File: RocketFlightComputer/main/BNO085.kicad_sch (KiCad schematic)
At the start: 10 parts

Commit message: Well I added a bunch of sensors, some connectors for battery, pyro channels mosfets, etc
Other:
- note added: "Max Current: 30 mA"
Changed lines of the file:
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@@
     (stroke (width 0) (type default))
+  )
+  (text "Max Current: 30 mA" (at 93.98 99.06 0)
+    (effects (font (size 1.778 1.5113)) (justify left bottom))
   )
   (text "SA0 is default low, so I2C ADDR = 1001010 (0x4A)" (at 94.615 103.505 0)

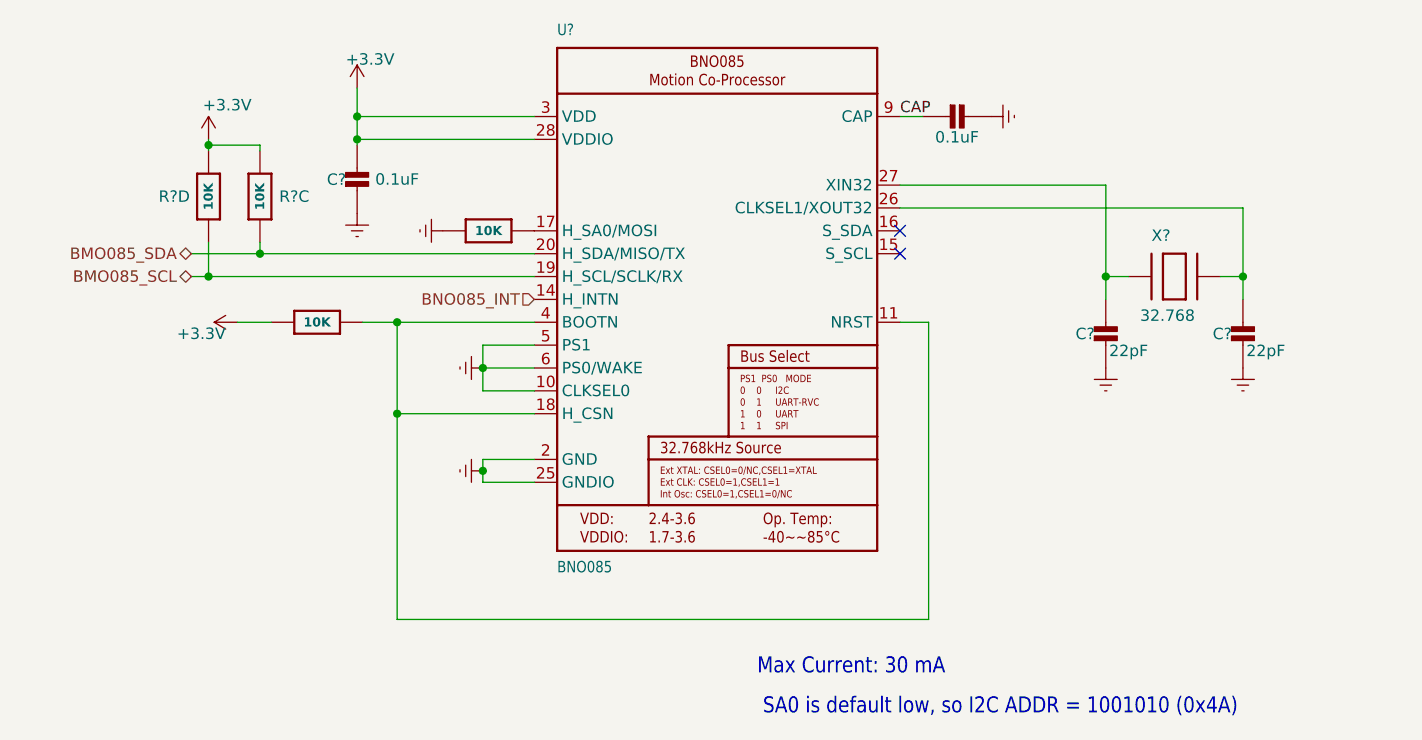
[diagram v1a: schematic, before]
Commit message: Addition of telemetry is pcb schematic
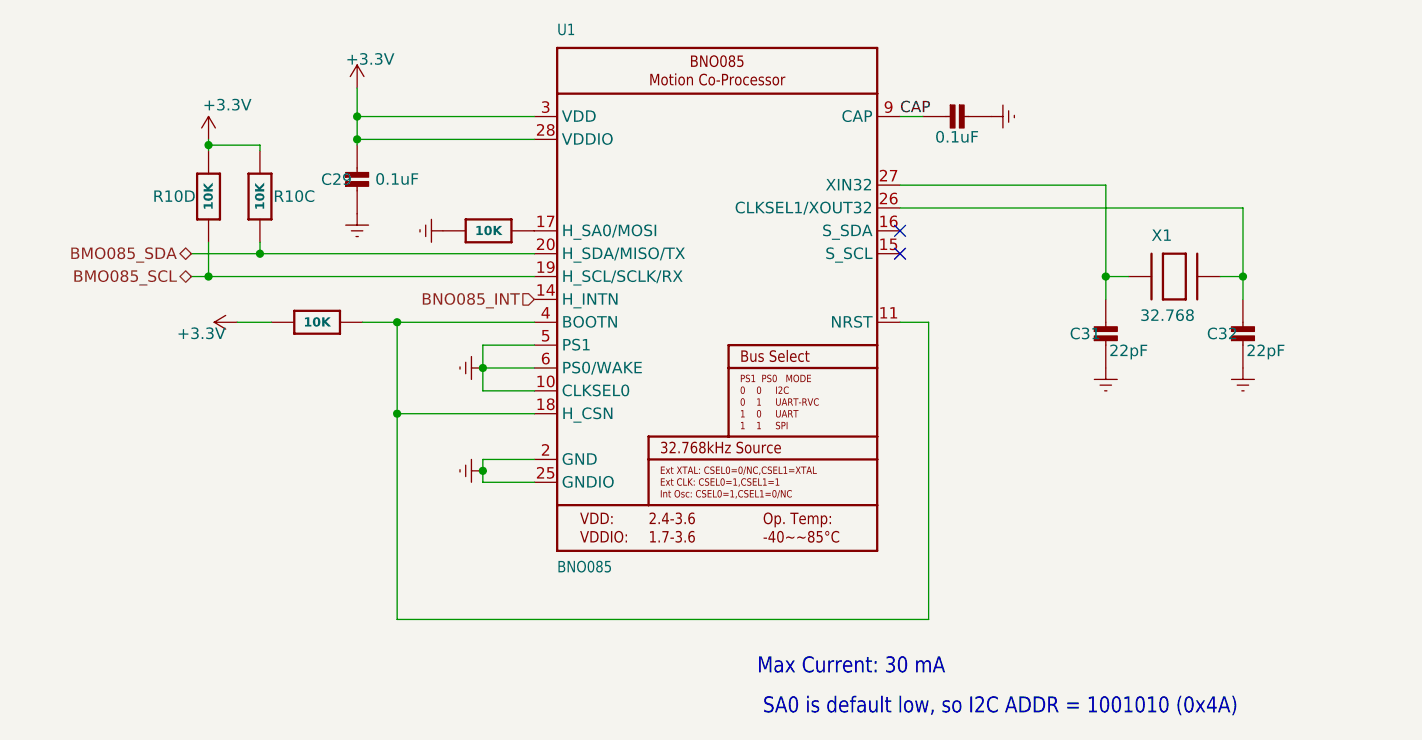
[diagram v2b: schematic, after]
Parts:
- gave numbers to parts that had none: 8

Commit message: The design is getting more mature, still did not choose if doing 4 layers or 2 layers pcb, will try to add 5v for a on board camera and trace routes for reserved pins in case of usage on another vehicle
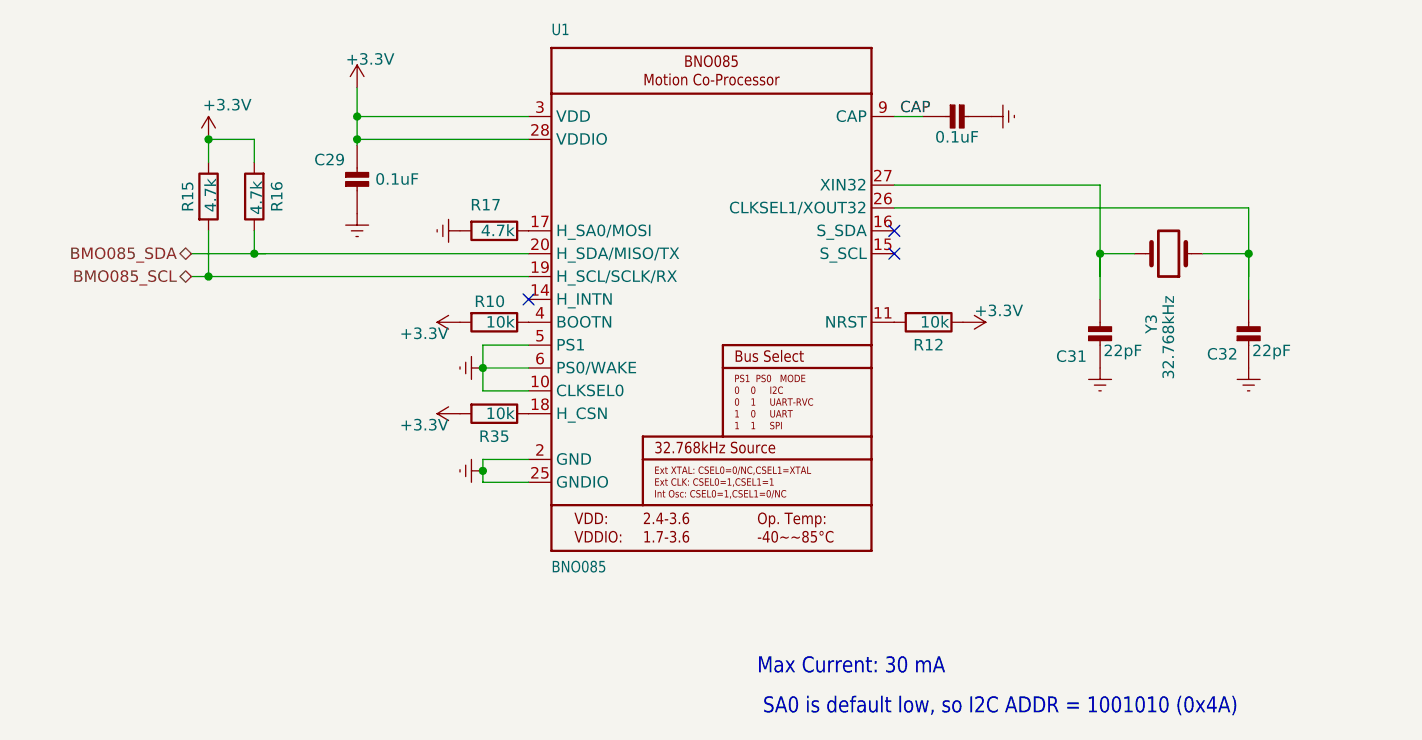
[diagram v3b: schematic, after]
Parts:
- removed R10, R11: 10K, Resistor_SMD:R_0603_1608Metric_Pad0.98x0.95mm_HandSolder, symbol Adafruit_BNO08x-eagle-import:RESISTOR_4PACK
- removed X1: 32.768, Crystal:Crystal_SMD_2012-2Pin_2.0x1.2mm, symbol Adafruit_BNO08x-eagle-import:XTAL-3.2X1.5
- added R10, R12, R35: 10k, Resistor_SMD:R_0603_1608Metric_Pad0.98x0.95mm_HandSolder, symbol Device:R
- added R15, R16, R17: 4.7k, Resistor_SMD:R_0603_1608Metric_Pad0.98x0.95mm_HandSolder, symbol Device:R
- added Y3: 32.768kHz, Crystal:Crystal_SMD_2012-2Pin_2.0x1.2mm, symbol Device:Crystal
- C32: footprint Adafruit_BNO08x:0603-NO -> Resistor_SMD:R_0603_1608Metric_Pad0.98x0.95mm_HandSolder
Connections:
- net +3.3V: now also R10.2, R12.1, R15.1, R16.2, R35.2
- net BMO085_SCL: now also R15.2
- net BMO085_SDA: now also R16.1
- net GNDREF: now also R17.2
- net at C31.1, U1.27 (XIN32): now also Y3.2
- net at C32.1, U1.26 (CLKSEL1/XOUT32): now also Y3.1
- net at U1.17 (H_SA0/MOSI): now also R17.1
- net BNO085_INT: no longer names the net of U1.14 (H_INTN)
- new net: R12.2, U1.11 (NRST)
- new net: R10.1, U1.4 (BOOTN)
- new net: R35.1, U1.18 (H_CSN)
- no-connect marks 2 -> 3
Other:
- moved on the sheet: C31, C32, U1

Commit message: Layout of PCB mostly done
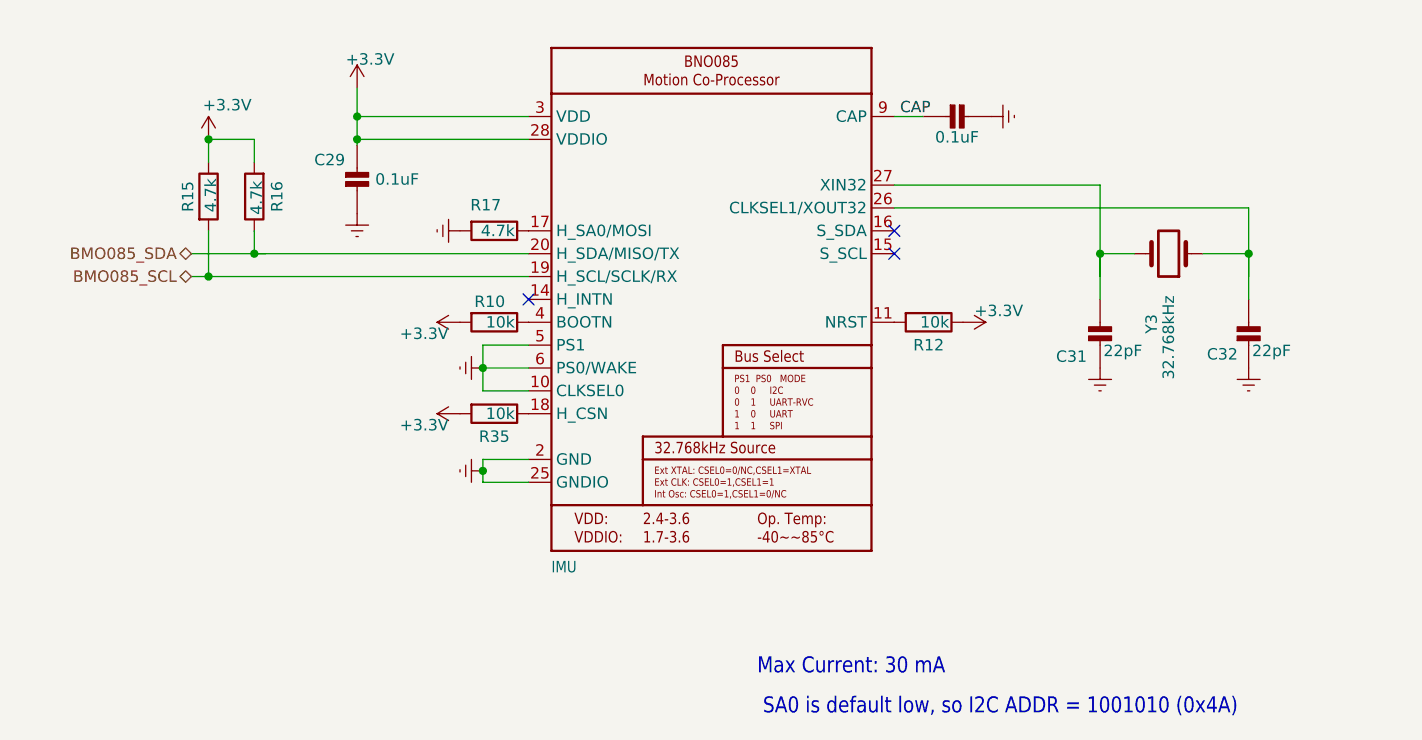
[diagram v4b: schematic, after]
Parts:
- BNO85: renamed from U1; value BNO085 -> IMU; footprint BNO08x:BNO080 -> footprint:BNO085
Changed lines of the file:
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@@
 		(on_board yes)
 		(dnp no)
-		(property "Reference" "U1"
+		(property "Reference" "BNO85"
 			(at 71.12 27.94 0)
 			(effects
@@
 				)
 				(justify left bottom)
+				(hide yes)
 			)
 		)
-		(property "Value" "BNO085"
+		(property "Value" "IMU"
 			(at 71.12 87.63 0)
 			(effects
@@
 			)
 		)
-		(property "Footprint" "BNO08x:BNO080"
+		(property "Footprint" "footprint:BNO085"
 			(at 88.9 57.15 0)
 			(effects
@@
 			(project "main"
 				(path "/27195d1d-92b2-40df-ada5-3b20841577e7/f1ce41f5-ec33-4382-82d9-21de8266ebc9"
-					(reference "U1")
+					(reference "BNO85")
 					(unit 1)
 				)

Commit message: Preliminary layout done but need to rearrange sd card and such to have the best routing
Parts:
- Y3: footprint Crystal:Crystal_SMD_2012-2Pin_2.0x1.2mm -> footprint:830050789
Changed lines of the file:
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@@
 			)
 		)
-		(property "Footprint" "Crystal:Crystal_SMD_2012-2Pin_2.0x1.2mm"
+		(property "Footprint" "footprint:830050789"
 			(at 139.7 52.07 0)
 			(effects

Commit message: Routing pcb
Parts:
- Y3: footprint footprint:830050789 -> Crystal:Crystal_SMD_2012-2Pin_2.0x1.2mm_HandSoldering
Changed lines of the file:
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@@
 			)
 		)
-		(property "Footprint" "footprint:830050789"
+		(property "Footprint" "Crystal:Crystal_SMD_2012-2Pin_2.0x1.2mm_HandSoldering"
 			(at 139.7 52.07 0)
 			(effects

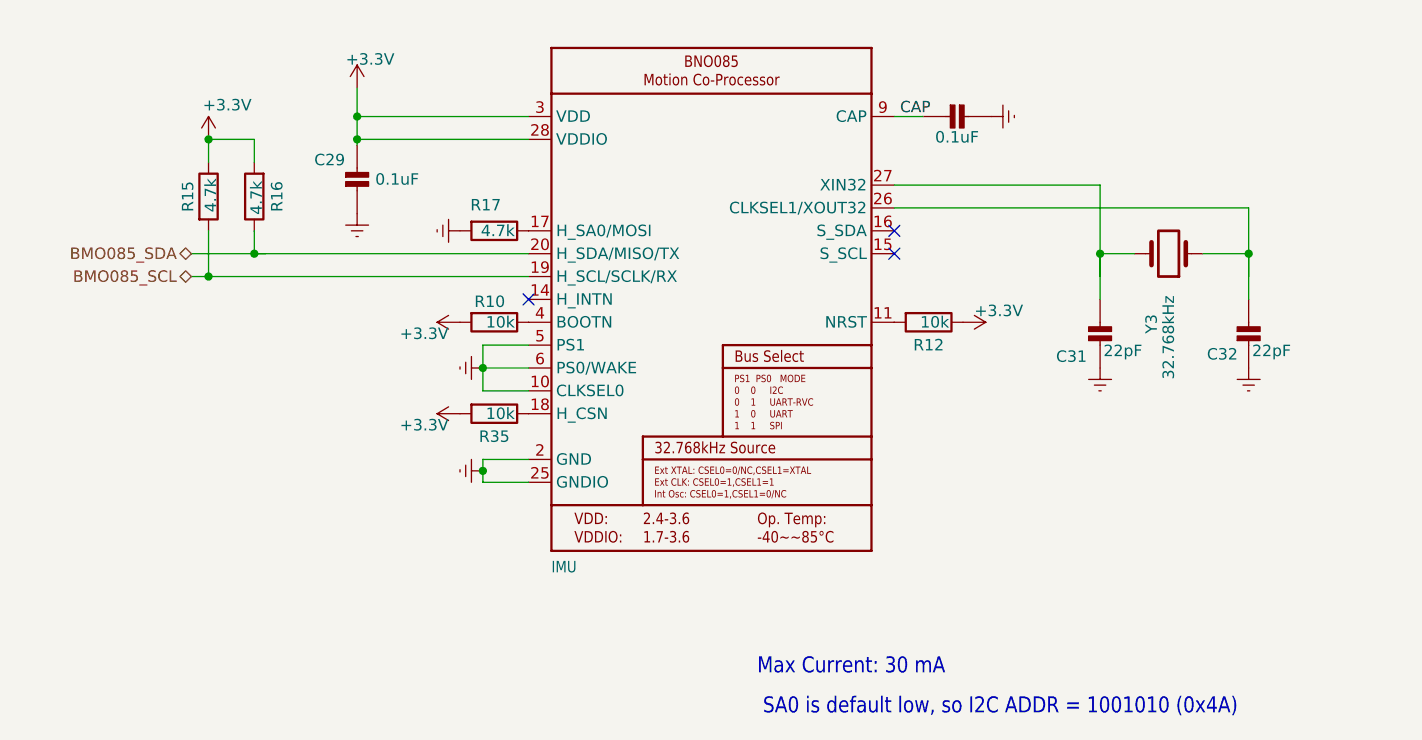
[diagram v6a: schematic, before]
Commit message: Addition of teensy example and milestone on routing completed, missing a few components to connect
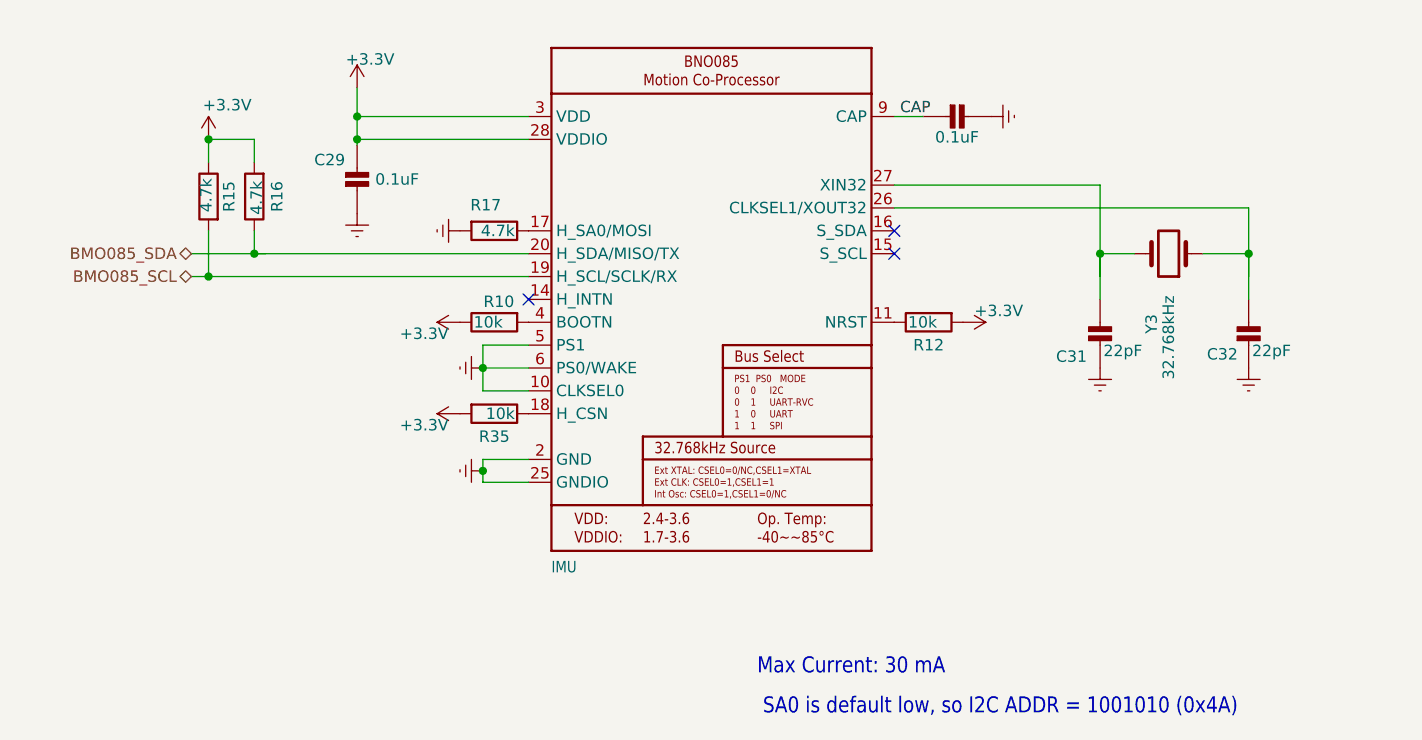
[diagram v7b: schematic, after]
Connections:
- net +3.3V: now also R10.1, R12.2; no longer R10.2, R12.1
- net at BNO85.11 (NRST): now also R12.1; no longer R12.2
- net at BNO85.4 (BOOTN): now also R10.2; no longer R10.1
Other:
- moved on the sheet: R10, R12
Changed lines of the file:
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@@
 	(symbol
 		(lib_id "Device:R")
-		(at 113.03 59.69 270)
+		(at 113.03 59.69 90)
+		(mirror x)
 		(unit 1)
 		(exclude_from_sim no)
@@
 		)
 		(property "Value" "10k"
-			(at 115.316 59.69 90)
+			(at 110.744 59.69 90)
 			(effects
 				(font
@@
 	(symbol
 		(lib_id "Device:R")
-		(at 64.77 59.69 270)
+		(at 64.77 59.69 90)
+		(mirror x)
 		(unit 1)
 		(exclude_from_sim no)
@@
 		(dnp no)
 		(property "Reference" "R10"
-			(at 64.262 57.404 90)
+			(at 65.278 57.404 90)
 			(effects
 				(font
@@
 		)
 		(property "Value" "10k"
-			(at 67.056 59.69 90)
+			(at 62.484 59.69 90)
 			(effects
 				(font
@@
 		(lib_id "Device:R")
 		(at 33.02 45.72 0)
+		(mirror y)
 		(unit 1)
 		(exclude_from_sim no)
@@
 		(dnp no)
 		(property "Reference" "R15"
-			(at 30.734 45.72 90)
+			(at 35.306 45.72 90)
 			(effects
 				(font
@@
 		)
 		(property "Value" "4.7k"
-			(at 33.274 43.688 90)
+			(at 32.766 43.688 90)
 			(effects
 				(font
@@
 		)
 		(property "Footprint" "Resistor_SMD:R_0603_1608Metric_Pad0.98x0.95mm_HandSolder"
-			(at 31.242 45.72 90)
-			(effects
-				(font
+			(at 34.798 45.72 90)
+			(effects
+				(font

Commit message: First pass of verification and validation of pcb design
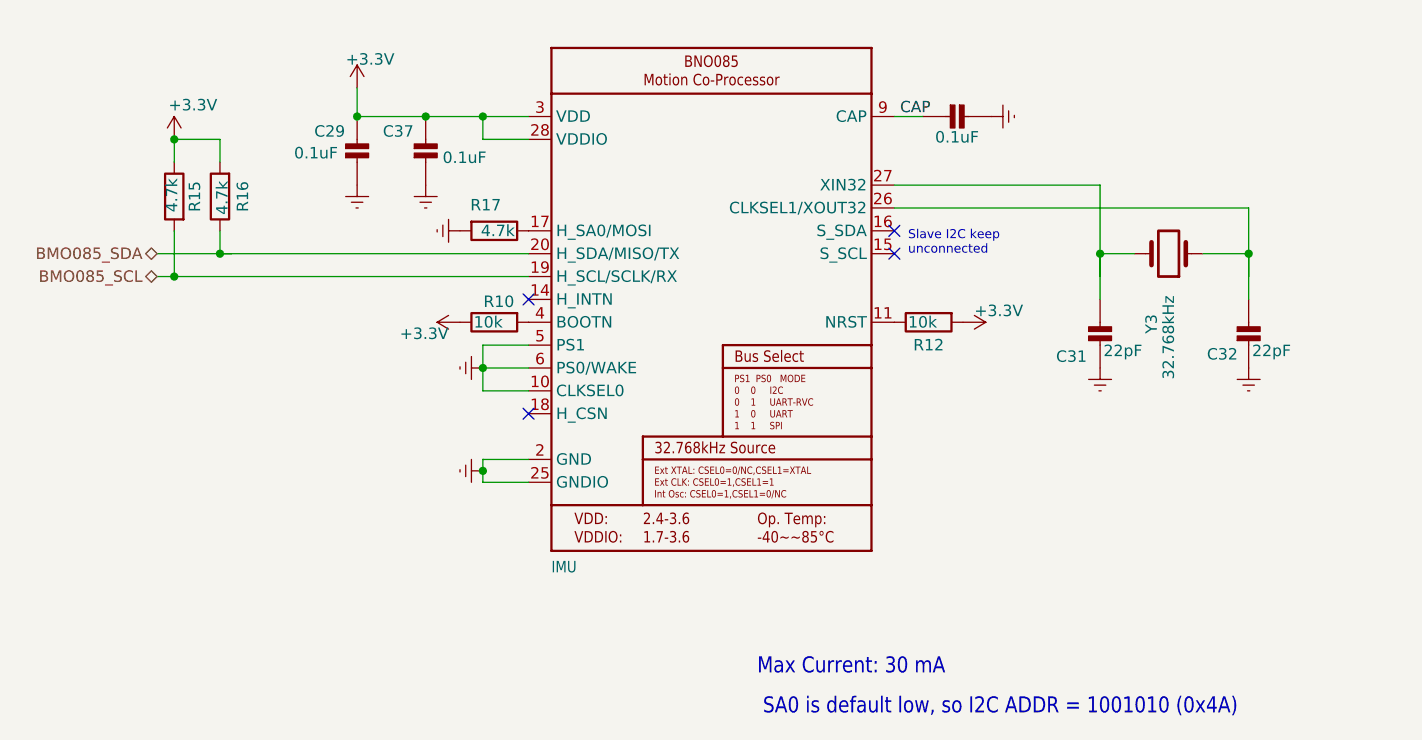
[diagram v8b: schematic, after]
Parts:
- removed R35: 10k, Resistor_SMD:R_0603_1608Metric_Pad0.98x0.95mm_HandSolder, symbol Device:R
- added C37: 0.1uF, Resistor_SMD:R_0603_1608Metric_Pad0.98x0.95mm_HandSolder, symbol Adafruit_BNO08x-eagle-import:CAP_CERAMIC0603_NO
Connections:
- net +3.3V: now also C37.1
- net GNDREF: now also C37.2
- no-connect marks 3 -> 4
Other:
- note added: "Slave I2C keep unconnected"
- moved on the sheet: C29, R15, R16
